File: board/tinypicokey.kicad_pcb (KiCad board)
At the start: 2 copper layers, 18 x 21 mm, 3 parts, among them SW1 SW_Push, U1 tiny2040

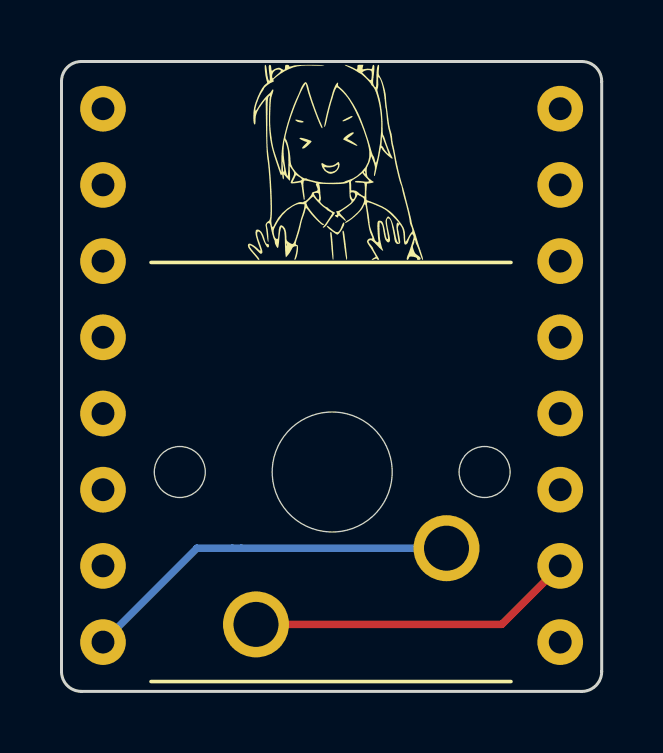
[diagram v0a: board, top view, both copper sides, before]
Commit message: Rev.2
* resize through holes from 0.7mm to 1.02mm
* add strap hole
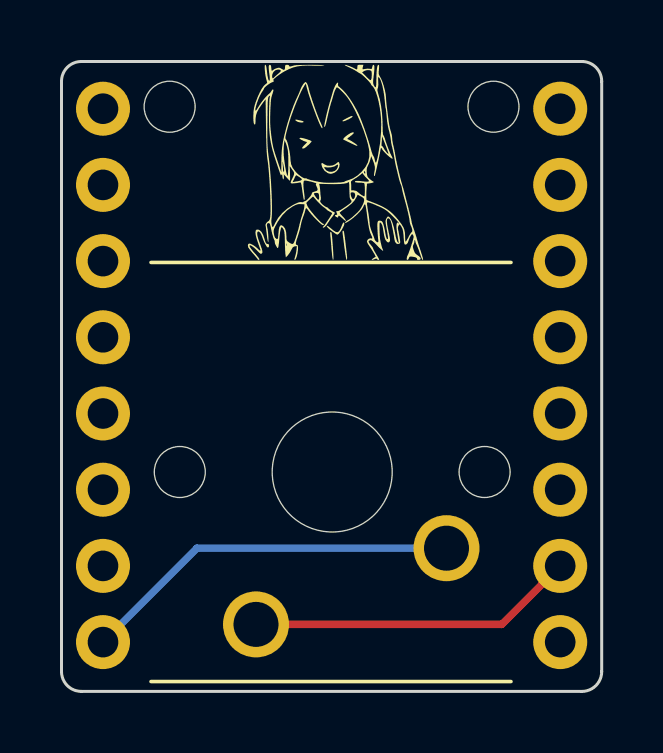
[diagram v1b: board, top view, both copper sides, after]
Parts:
- added ?: , , F.Cu at (107.7, 79.0)
- added ?: , , F.Cu at (96.9, 79.0)
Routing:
- net Net-(SW1-Pad1): track 11.6 -> 10.9 mm
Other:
- board text added: "TinyPicoKey Rev.2 2021 @Akkiesoft"
- board text removed: "TinyPicoKey Rev.1 2021 @Akkiesoft"

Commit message: Rev.3
* expanded the strap hole
* change board image
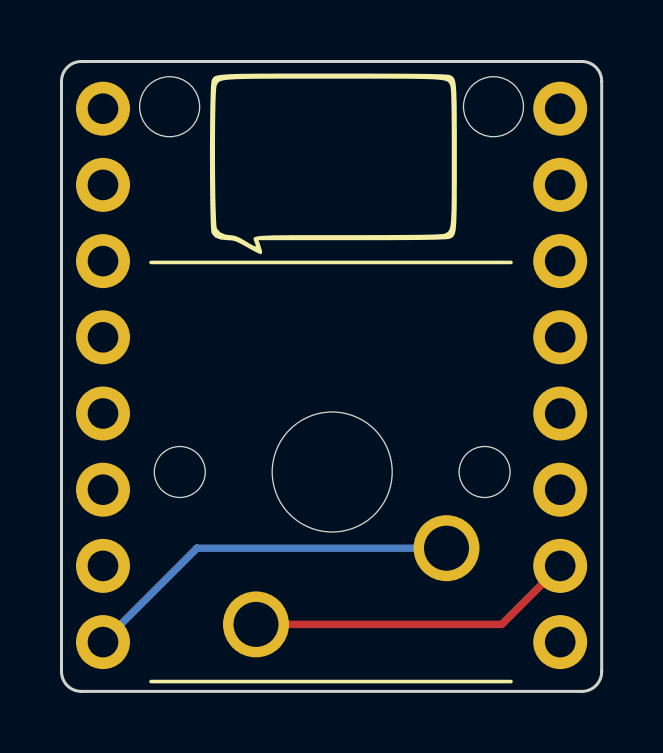
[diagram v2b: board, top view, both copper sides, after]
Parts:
- removed the ? at (99.7, 79.1)
- added G***: Fukidashi, Library:Fukidashi, F.Cu at (102.4, 80.9)
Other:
- board text added: "TinyPicoKey Rev.3 2022 @Akkiesoft"
- board text removed: "TinyPicoKey Rev.2 2021 @Akkiesoft"
